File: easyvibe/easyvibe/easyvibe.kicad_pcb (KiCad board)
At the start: 2 copper layers, 111 x 54.6 mm, 82 parts, among them U1 TL062, U2 TL062, U3 TL062, U4 TL062

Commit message: add ground fill on edge
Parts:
- moved R5 1.28 mm to (35.1, 109.6)
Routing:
- added copper zone on B.Cu, net GND
- added copper zone on F.Cu, net GND
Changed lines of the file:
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@@
 	(footprint "Snapeda:YAG_MF25_YAG"
 		(layer "F.Cu")
-		(at 34.798 110.8583)
+		(at 35.052 109.601)
 		(tags "MFR-25FRF52-10K ")
 		(property "Reference" "R5"
@@
 		(layer "Edge.Cuts")
 	)
+	(zone
+		(net "GND")
+		(layers "F.Cu" "B.Cu")
+		(hatch edge 0.5)
+		(priority 1)
+		(connect_pads
+			(clearance 0.5)
+		)
+		(min_thickness 0.25)
+		(fill
+			(thermal_gap 0.5)
+			(thermal_bridge_width 0.5)
+			(island_removal_mode 0)
+		)
+		(polygon
+			(pts
+				(xy 45.847 91.186) (xy 142.113 91.186) (xy 142.113 92.456) (xy 45.847 92.329)
+			)
+		)
+	)
+	(zone
+		(net "GND")
+		(layers "F.Cu" "B.Cu")
+		(hatch edge 0.5)
+		(priority 2)
+		(connect_pads
+			(clearance 0.5)
+		)
+		(min_thickness 0.25)
+		(fill
+			(thermal_gap 0.5)
+			(thermal_bridge_width 0.5)
+			(island_removal_mode 0)
+		)
+		(polygon
+			(pts
+				(xy 148.717 85.217) (xy 147.32 85.217) (xy 147.32 45.847) (xy 148.717 45.847)
+			)
+		)
+	)
+	(zone
+		(net "GND")
+		(layers "F.Cu" "B.Cu")
+		(hatch edge 0.5)
+		(connect_pads
+			(clearance 0.5)
+		)
+		(min_thickness 0.25)
+		(fill
+			(thermal_gap 0.5)
+			(thermal_bridge_width 0.5)
+			(island_removal_mode 0)
+		)
+		(polygon
+			(pts
+				(xy 39.116 47.117) (xy 40.132 47.117) (xy 40.132 85.471) (xy 38.989 85.344)
+			)
+		)
+	)
 	(embedded_fonts no)

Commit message: initial component placement everywheres
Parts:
- removed J_DRIVE1, J_DRIVE2, J_DRIVE3: C, Connector_PinSocket_2.54mm:PinSocket_1x01_P2.54mm_Vertical
- added R24: 1K, Snapeda:RES_LR1_TYCO_TYC, F.Cu at (112.8, 51.5)
- LDR1, LDR2, LDR3, LDR4: footprint OptoDevice:R_LDR_10x8.5mm_P7.6mm_Vertical -> Snapeda:TO_NSL_19M_ADP
- moved R14 141.7 mm to (141.1, 55.6), turned to -90 degrees
- moved J_RATE2 139.1 mm to (130.7, 41.5)
- moved J_IN_SLV1 135.5 mm to (48.4, 41.7)
- moved DRIVE1 134.0 mm to (117.3, 53.9), turned to 90 degrees
- moved J_RATE1 133.0 mm to (125.9, 41.8)
- moved R21 132.6 mm to (134.1, 40.7), turned to -90 degrees
- moved J_VIB3 132.1 mm to (79.4, 41.9)
- moved J_STOMP_1 131.7 mm to (43.9, 49.8), turned to 90 degrees
- moved J_DEPTH_1 131.6 mm to (85.7, 41.9)
- moved J_DEPTH3 128.9 mm to (100.5, 41.9)
- moved J_VIB2 128.3 mm to (74.2, 41.9)
- moved J_IN_Ring1 128.1 mm to (62.5, 41.8)
- moved D4 125.9 mm to (81.3, 45.6), turned to 90 degrees
- moved J_Batt_Pos1 124.8 mm to (118.1, 41.8)
- moved J_VIB1 124.7 mm to (69.0, 41.9)
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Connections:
- U3 pad 3: Net-(J_DEPTH2-Pin_1) -> Net-(U3A-+)
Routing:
- net (no net): track 0.00 -> 26.4 mm

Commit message: some fixes
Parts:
- moved D2 3.18 mm to (77.5, 57.6)
- moved D4 0.65 mm to (81.4, 45.0)
- moved R15 0.52 mm to (70.2, 44.8)
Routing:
- net (no net): track 26.4 -> 27.2 mm
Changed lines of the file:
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@@
 	(footprint "Snapeda:AFL-W2C8.9D"
 		(layer "F.Cu")
-		(at 81.28 45.61332 90)
+		(at 81.407 44.97832 90)
 		(tags "1N914 ")
 		(property "Reference" "D4"
@@
 	(footprint "Snapeda:YAG_MF25_YAG"
 		(layer "F.Cu")
-		(at 70.104 44.323 -90)
+		(at 70.231 44.831 -90)
 		(tags "MFR-25FRF52-10K ")
 		(property "Reference" "R15"
@@
 	(footprint "Snapeda:AFL-W2C8.9D"
 		(layer "F.Cu")
-		(at 77.597 54.46268 -90)
+		(at 77.47 57.63768 -90)
 		(tags "1N914 ")
 		(property "Reference" "D2"
@@
 	)
 	(segment
-		(start 139.7 91.186)
-		(end 139.7 88.011)
+		(start 41.402 82.042)
+		(end 39.497 82.042)
 		(width 0.2)
 		(layer "F.Cu")
@@
 	)
 	(segment
-		(start 41.402 82.042)
-		(end 47.625 88.265)
+		(start 139.7 91.186)
+		(end 139.7 88.011)
 		(width 0.2)
 		(layer "F.Cu")
@@
 	)
 	(segment
-		(start 47.625 91.186)
-		(end 47.752 91.313)
+		(start 47.625 88.265)
+		(end 41.402 82.042)
 		(width 0.2)
 		(layer "F.Cu")
@@
 	)
 	(segment
-		(start 47.625 88.265)
-		(end 47.625 91.186)
+		(start 47.625 91.186)
+		(end 47.625 88.265)
 		(width 0.2)
 		(layer "F.Cu")
@@
 	)
 	(segment
-		(start 40.259 82.042)
-		(end 41.402 82.042)
+		(start 139.7 88.011)
+		(end 145.034 82.677)
 		(width 0.2)
 		(layer "F.Cu")
@@
 	)
 	(segment
-		(start 139.7 88.011)
-		(end 145.034 82.677)
+		(start 47.752 91.313)
+		(end 47.625 91.186)
 		(width 0.2)
 		(layer "F.Cu")
@@
 		)
 		(min_thickness 0.25)
-		(fill
+		(fill yes
 			(thermal_gap 0.5)
 			(thermal_bridge_width 0.5)
@@
 		)
 		(min_thickness 0.25)
-		(fill
+		(fill yes
 			(thermal_gap 0.5)
 			(thermal_bridge_width 0.5)
@@
 		)
 		(min_thickness 0.25)
-		(fill
+		(fill yes
 			(thermal_gap 0.5)
 			(thermal_bridge_width 0.5)

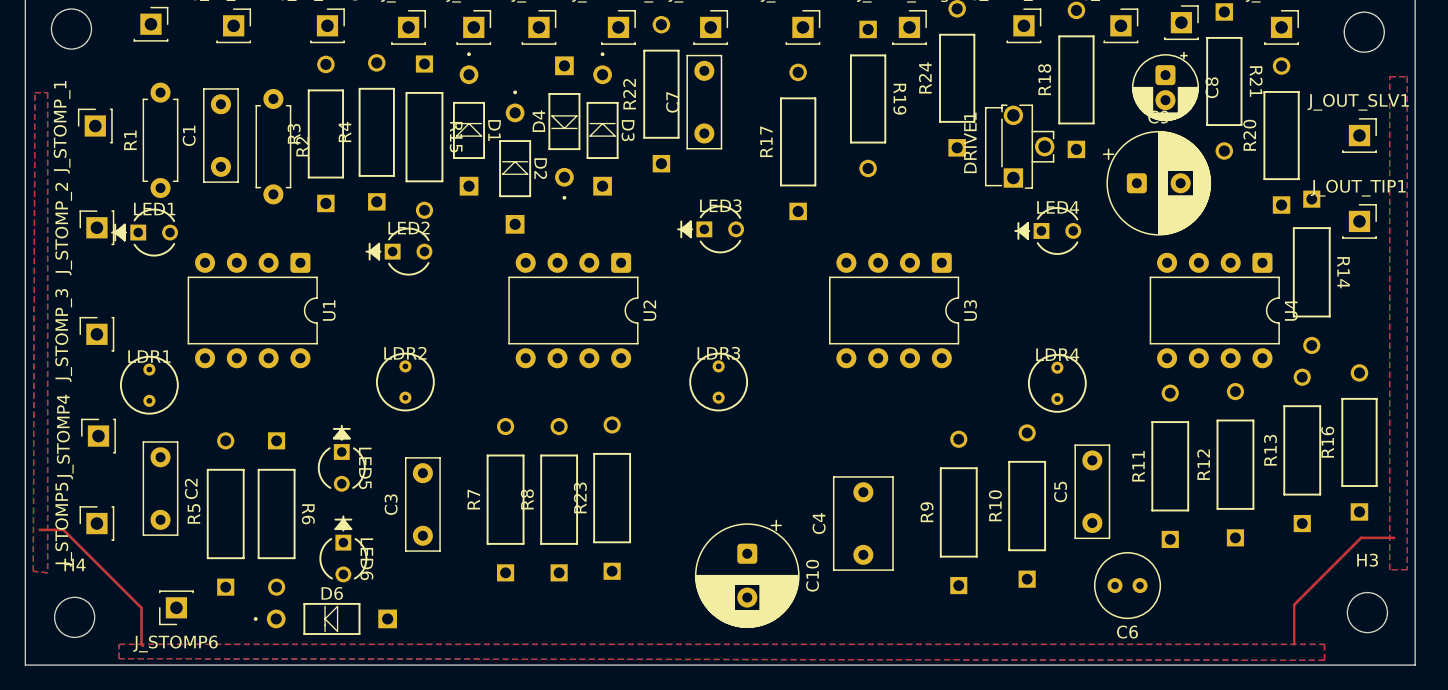
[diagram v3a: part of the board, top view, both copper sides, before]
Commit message: fix ground fill
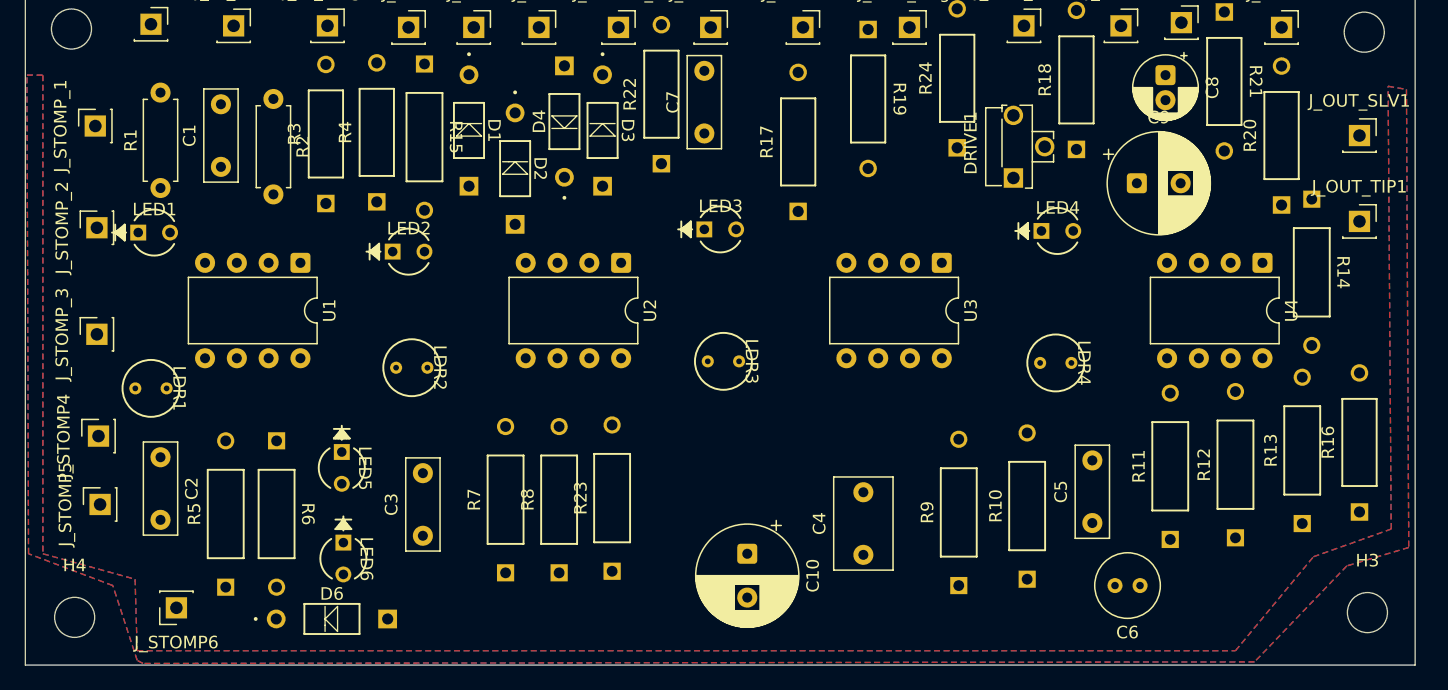
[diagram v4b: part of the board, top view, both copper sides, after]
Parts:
- moved LDR1 2.04 mm to (49.6, 70.7), turned to -90 degrees
- moved LDR2 1.76 mm to (70.5, 69.1), turned to -90 degrees
- moved LDR3 1.68 mm to (95.4, 68.6), turned to -90 degrees
- moved J_STOMP5 1.55 mm to (44.3, 80.0)
- moved LDR4 1.19 mm to (121.9, 68.7), turned to -90 degrees
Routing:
- net (no net): track 27.2 -> 0.00 mm

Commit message: ff
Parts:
- moved C7 1.28 mm to (93.9, 50.3)
- moved J_STOMP_2 0.51 mm to (43.6, 57.9)
- moved DRIVE1 0.36 mm to (117.0, 54.2)
- moved D3 0.13 mm to (84.6, 54.6)
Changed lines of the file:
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@@
 	(footprint "Connector_PinSocket_2.54mm:PinSocket_1x01_P2.54mm_Vertical"
 		(layer "F.Cu")
-		(at 44.069 57.912 90)
+		(at 43.561 57.912 90)
 		(descr "Through hole straight socket strip, 1x01, 2.54mm pitch, single row (from Kicad 4.0.7), script generated")
 		(tags "Through hole socket strip THT 1x01 2.54mm single row")
@@
 	(footprint "Potentiometer_THT:Potentiometer_Runtron_RM-063_Horizontal"
 		(layer "F.Cu")
-		(at 117.266 53.935 90)
+		(at 117.012 54.189 90)
 		(descr "Potentiometer, horizontal, Trimmer, RM-063 http://www.runtron.com/down/PDF%20Datasheet/Carbon%20Film%20Potentiometer/RM065%20RM063.pdf")
 		(tags "Potentiometer Trimmer RM-063")
@@
 	(footprint "Capacitor_THT:C_Rect_L7.2mm_W2.5mm_P5.00mm_FKS2_FKP2_MKS2_MKP2"
 		(layer "F.Cu")
-		(at 92.583 50.379 90)
+		(at 93.853 50.252 90)
 		(descr "C, Rect series, Radial, pin pitch=5.00mm, length*width=7.2*2.5mm^2, Capacitor, http://www.wima.com/EN/WIMA_FKS_2.pdf")
 		(tags "C Rect series Radial pin pitch 5.00mm length 7.2mm width 2.5mm Capacitor")
@@
 	(footprint "Snapeda:AFL-W2C8.9D"
 		(layer "F.Cu")
-		(at 84.455 54.58968 -90)
+		(at 84.582 54.58968 -90)
 		(tags "1N914 ")
 		(property "Reference" "D3"

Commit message: some fixes
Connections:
- C2 pad 2: Net-(U1B--) -> Net-(U1B-+)
- C3 pad 2: Net-(U2B--) -> Net-(U2B-+)
- C4 pad 2: Net-(U3B--) -> Net-(U3B-+)
- C5 pad 2: Net-(U4B--) -> Net-(U4B-+)
- C6 pad 1: Net-(J_STOMP5-Pin_1) -> Net-(C6-Pad1)
- C6 pad 2: Net-(C6-Pad2) -> Net-(J_STOMP5-Pin_1)
- C8 pad 1: Net-(C8-Pad1) -> Net-(J_RATE1-Pin_1)
- LDR1 pad 1: Net-(U1B--) -> Net-(U1B-+)
- LDR2 pad 1: Net-(U2B--) -> Net-(U2B-+)
- LDR3 pad 1: Net-(U3B--) -> Net-(U3B-+)
- LDR4 pad 1: Net-(U4B--) -> Net-(U4B-+)
- R10 pad 1: Net-(U3B-+) -> Net-(U3B--)
- R11 pad 2: Net-(U4B-+) -> Net-(U4B--)
- R12 pad 1: Net-(U4B-+) -> Net-(U4B--)
- R13 pad 1: Net-(C6-Pad2) -> Net-(C6-Pad1)
- R14 pad 2: Net-(C6-Pad2) -> Net-(C6-Pad1)
- R20 pad 2: Net-(C8-Pad1) -> Net-(J_RATE1-Pin_1)
- R5 pad 2: Net-(U1B-+) -> Net-(U1B--)
- R6 pad 1: Net-(U1B-+) -> Net-(U1B--)
- R7 pad 2: Net-(U2B-+) -> Net-(U2B--)
- R8 pad 1: Net-(U2B-+) -> Net-(U2B--)
- R9 pad 2: Net-(U3B-+) -> Net-(U3B--)
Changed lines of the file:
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@@
 			(layers "*.Cu" "*.Mask")
 			(remove_unused_layers no)
-			(net "Net-(U3B-+)")
+			(net "Net-(U3B--)")
 			(pintype "passive")
 		)
@@
 			(layers "*.Cu" "*.Mask")
 			(remove_unused_layers no)
-			(net "Net-(U4B--)")
+			(net "Net-(U4B-+)")
 			(pintype "passive")
 		)
@@
 			(layers "*.Cu" "*.Mask")
 			(remove_unused_layers no)
-			(net "Net-(C8-Pad1)")
+			(net "Net-(J_RATE1-Pin_1)")
 			(pintype "passive")
 		)
@@
 			(layers "*.Cu" "*.Mask")
 			(remove_unused_layers no)
-			(net "Net-(U1B-+)")
+			(net "Net-(U1B--)")
 			(pintype "passive")
 		)
@@
 			(layers "*.Cu" "*.Mask")
 			(remove_unused_layers no)
-			(net "Net-(U2B--)")
+			(net "Net-(U2B-+)")
 			(pintype "passive")
 		)
@@
 			(layers "*.Cu" "*.Mask")
 			(remove_unused_layers no)
-			(net "Net-(U1B-+)")
+			(net "Net-(U1B--)")
 			(pintype "passive")
 		)
@@
 			(layers "*.Cu" "*.Mask")
 			(remove_unused_layers no)
-			(net "Net-(C6-Pad2)")
+			(net "Net-(C6-Pad1)")
 			(pintype "passive")
 		)
@@
 			(layers "*.Cu" "*.Mask")
 			(remove_unused_layers no)
-			(net "Net-(J_STOMP5-Pin_1)")
+			(net "Net-(C6-Pad1)")
 			(pintype "passive")
 		)
@@
 			(layers "*.Cu" "*.Mask")
 			(remove_unused_layers no)
-			(net "Net-(C6-Pad2)")
+			(net "Net-(J_STOMP5-Pin_1)")
 			(pintype "passive")
 		)
@@
 			(layers "*.Cu" "*.Mask")
 			(remove_unused_layers no)
-			(net "Net-(C6-Pad2)")
+			(net "Net-(C6-Pad1)")
 			(pintype "passive")
 		)
@@
 			(layers "*.Cu" "*.Mask")
 			(remove_unused_layers no)
-			(net "Net-(U3B-+)")
+			(net "Net-(U3B--)")
 			(pintype "passive")
 		)
@@
 			(layers "*.Cu" "*.Mask")
 			(remove_unused_layers no)
-			(net "Net-(U4B--)")
+			(net "Net-(U4B-+)")
 			(pintype "passive")
 		)
@@
 			(layers "*.Cu" "*.Mask")
 			(remove_unused_layers no)
-			(net "Net-(U1B--)")
+			(net "Net-(U1B-+)")
 			(pintype "passive")
 		)
@@
 			(layers "*.Cu" "*.Mask")
 			(remove_unused_layers no)
-			(net "Net-(U4B-+)")
+			(net "Net-(U4B--)")
 			(pintype "passive")
 		)
@@
 			(layers "*.Cu" "*.Mask")
 			(remove_unused_layers no)
-			(net "Net-(U2B--)")
+			(net "Net-(U2B-+)")
 			(pintype "passive")
 		)
@@
 			(layers "*.Cu" "*.Mask")
 			(remove_unused_layers no)
-			(net "Net-(U1B--)")
+			(net "Net-(U1B-+)")
 			(pintype "passive")
 		)
@@
 			(layers "*.Cu" "*.Mask")
 			(remove_unused_layers no)
-			(net "Net-(U4B-+)")
+			(net "Net-(U4B--)")
 			(pintype "passive")
 		)
@@
 			(remove_unused_layers no)
 			(roundrect_rratio 0.15625)
-			(net "Net-(C8-Pad1)")
+			(net "Net-(J_RATE1-Pin_1)")
 			(pintype "passive")
 		)
@@
 			(layers "*.Cu" "*.Mask")
 			(remove_unused_layers no)
-			(net "Net-(U2B-+)")
+			(net "Net-(U2B--)")
 			(pintype "passive")
 		)
@@
 			(layers "*.Cu" "*.Mask")
 			(remove_unused_layers no)
-			(net "Net-(U2B-+)")
+			(net "Net-(U2B--)")
 			(pintype "passive")
 		)
@@
 			(layers "*.Cu" "*.Mask")
 			(remove_unused_layers no)
-			(net "Net-(U3B--)")
+			(net "Net-(U3B-+)")
 			(pintype "passive")
 		)
@@
 			(layers "*.Cu" "*.Mask")
 			(remove_unused_layers no)
-			(net "Net-(U3B--)")
+			(net "Net-(U3B-+)")
 			(pintype "passive")
 		)

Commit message: more tweaks, make board slightly smaller to fit box
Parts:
- removed R24: 1K, Snapeda:RES_LR1_TYCO_TYC
- moved U1 4.55 mm to (64.3, 63.0)
- moved LED1 3.42 mm to (49.9, 60.6)
- moved LED3 3.33 mm to (94.7, 60.6)
- moved DRIVE1 3.06 mm to (114.0, 54.4)
- moved LDR3 2.95 mm to (96.6, 71.2)
- moved U2 2.73 mm to (87.2, 63.1)
- moved LED4 2.73 mm to (120.8, 60.6)
- moved U3 2.73 mm to (112.8, 63.1)
- moved LDR4 2.65 mm to (122.7, 71.2)
- moved LDR2 2.50 mm to (71.7, 71.2)
- moved H3 2.45 mm to (144.7, 86.4)
- moved LED2 2.29 mm to (69.8, 60.6)
- moved LDR1 2.22 mm to (51.8, 71.2)
- moved H4 1.53 mm to (42.9, 87.6)
- moved H2 0.80 mm to (144.5, 42.5)
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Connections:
- C10 pad 1: Net-(D6-A) -> Net-(D2-K)
- D2 pad 1: Net-(D1-A) -> Net-(D2-K)
- D2 pad 2: Net-(D2-A) -> Net-(D1-K)
- D3 pad 1: Net-(D3-K) -> Net-(D1-A)
- D3 pad 2: Net-(D1-K) -> Net-(D3-A)
- D4 pad 1: Net-(D2-A) -> Net-(D3-A)
- D4 pad 2: Net-(D3-K) -> Net-(D2-K)
- D6 pad 2: Net-(D6-A) -> Net-(D2-K)
- J_DEPTH3 pad 1: Net-(D3-K) -> Net-(D2-K)
- J_DEPTH_1 pad 1: Net-(D1-K) -> Net-(D1-A)
- LDR1 pad 2: Net-(D6-A) -> Net-(D2-K)
- LDR2 pad 2: Net-(D6-A) -> Net-(D2-K)
- LDR3 pad 2: Net-(D6-A) -> Net-(D2-K)
- LDR4 pad 2: Net-(D6-A) -> Net-(D2-K)
- R15 pad 2: Net-(D6-A) -> Net-(D2-K)
- R17 pad 2: Net-(D1-K) -> Net-(D1-A)
- R2 pad 2: Net-(D6-A) -> Net-(D2-K)
- R21 pad 2: Net-(D2-A) -> Net-(D2-K)
- R23 pad 2: Net-(D6-A) -> Net-(D2-K)
- R3 pad 2: Net-(D6-A) -> Net-(D2-K)
- U2 pad 3: Net-(D6-A) -> Net-(D2-K)
- U3 pad 3: Net-(U3A-+) -> Net-(J_DEPTH2-Pin_1)
- U4 pad 2: Net-(D2-A) -> Net-(D2-K)
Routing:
- removed copper zone on B.Cu, net GND
- removed copper zone on F.Cu, net GND
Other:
- board size 111 x 54.6 mm -> 109.5 x 54 mm

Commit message: Added text
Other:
- board text added: "EasyAueVibe Rev. 0"
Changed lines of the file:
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@@
 		(layer "Edge.Cuts")
+	)
+	(gr_text "EasyAueVibe Rev. 0"
+		(at 69.088 91.694 0)
+		(layer "F.SilkS")
+		(effects
+			(font
+				(size 1 1)
+				(thickness 0.1)
+			)
+			(justify left bottom)
+		)
 	)
 	(embedded_fonts no)
